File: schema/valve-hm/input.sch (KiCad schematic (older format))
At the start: 5 parts, among them Q1 bc847

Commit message: Разводка платы.
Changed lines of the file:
@@
-EESchema Schematic File Version 2  date 15/06/2012 18:13:53
+EESchema Schematic File Version 2  date Sat 16 Jun 2012 11:54:35 AM MSK
 LIBS:power
 LIBS:device
@@
 Sheet 7 7
 Title ""
-Date "15 jun 2012"
+Date "16 jun 2012"
 Rev ""
 Comp ""
@@
 AR Path="/4FDB3921/4FDB399C" Ref="#PWR056"  Part="1"
 AR Path="/4FDB299D/4FDB399C" Ref="#PWR065"  Part="1"
-F 0 "#PWR065" H 5800 2150 30  0001 C CNN
+F 0 "#PWR050" H 5800 2150 30  0001 C CNN
 F 1 "VDD" H 5800 2160 30  0000 C CNN
 	1    5800 2050
@@
 AR Path="/4FDB3921/4FDB2AE7" Ref="R34"  Part="1"
 AR Path="/4FDB299D/4FDB2AE7" Ref="R42"  Part="1"
-F 0 "R42" V 5880 2550 50  0000 C CNN
+F 0 "R26" V 5880 2550 50  0000 C CNN
 F 1 "33k" V 5800 2550 50  0000 C CNN
 	1    5800 2550
@@
 AR Path="/4FDB3921/4FDB2AA4" Ref="R35"  Part="1"
 AR Path="/4FDB299D/4FDB2AA4" Ref="R43"  Part="1"
-F 0 "R43" V 6580 3250 50  0000 C CNN
+F 0 "R27" V 6580 3250 50  0000 C CNN
 F 1 "2k4" V 6500 3250 50  0000 C CNN
 	1    6500 3250
@@
 AR Path="/4FDB3921/4FDB2A6B" Ref="#PWR057"  Part="1"
 AR Path="/4FDB299D/4FDB2A6B" Ref="#PWR066"  Part="1"
-F 0 "#PWR066" H 4600 4700 30  0001 C CNN
+F 0 "#PWR051" H 4600 4700 30  0001 C CNN
 F 1 "GND" H 4600 4630 30  0001 C CNN
 	1    4600 4700
@@
 AR Path="/4FDB3921/4FDB2A62" Ref="#PWR058"  Part="1"
 AR Path="/4FDB299D/4FDB2A62" Ref="#PWR067"  Part="1"
-F 0 "#PWR067" H 5800 4550 30  0001 C CNN
+F 0 "#PWR052" H 5800 4550 30  0001 C CNN
 F 1 "GND" H 5800 4480 30  0001 C CNN
 	1    5800 4550
@@
 AR Path="/4FDB3921/4FDB29FE" Ref="R33"  Part="1"
 AR Path="/4FDB299D/4FDB29FE" Ref="R41"  Part="1"
-F 0 "R41" V 5130 3600 50  0000 C CNN
+F 0 "R25" V 5130 3600 50  0000 C CNN
 F 1 "2k4" V 5050 3600 50  0000 C CNN
 	1    5050 3600
@@
 AR Path="/4FDB3921/4FDB29E5" Ref="R32"  Part="1"
 AR Path="/4FDB299D/4FDB29E5" Ref="R40"  Part="1"
-F 0 "R40" V 4680 4250 50  0000 C CNN
+F 0 "R24" V 4680 4250 50  0000 C CNN
 F 1 "33k" V 4600 4250 50  0000 C CNN
 	1    4600 4250
@@
 AR Path="/4FDB3921/4FDB29D2" Ref="Q3"  Part="1"
 AR Path="/4FDB299D/4FDB29D2" Ref="Q8"  Part="1"
-F 0 "Q8" H 5700 3450 50  0000 R CNN
+F 0 "Q1" H 5700 3450 50  0000 R CNN
 F 1 "bc847" H 5700 3750 50  0000 R CNN
 	1    5700 3600

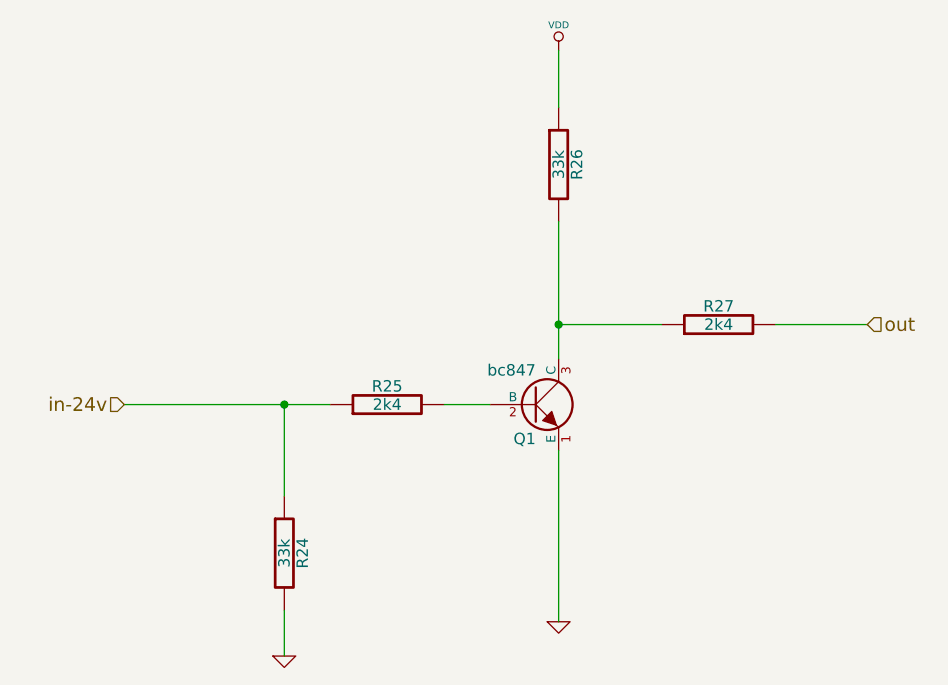
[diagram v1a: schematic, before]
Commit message: Valve-hm is ready. It's digital IO board which can control up to 20 io pins. It is rquipt with 3 LEDs, 2 operating mode switches, USB port and TWI interface.
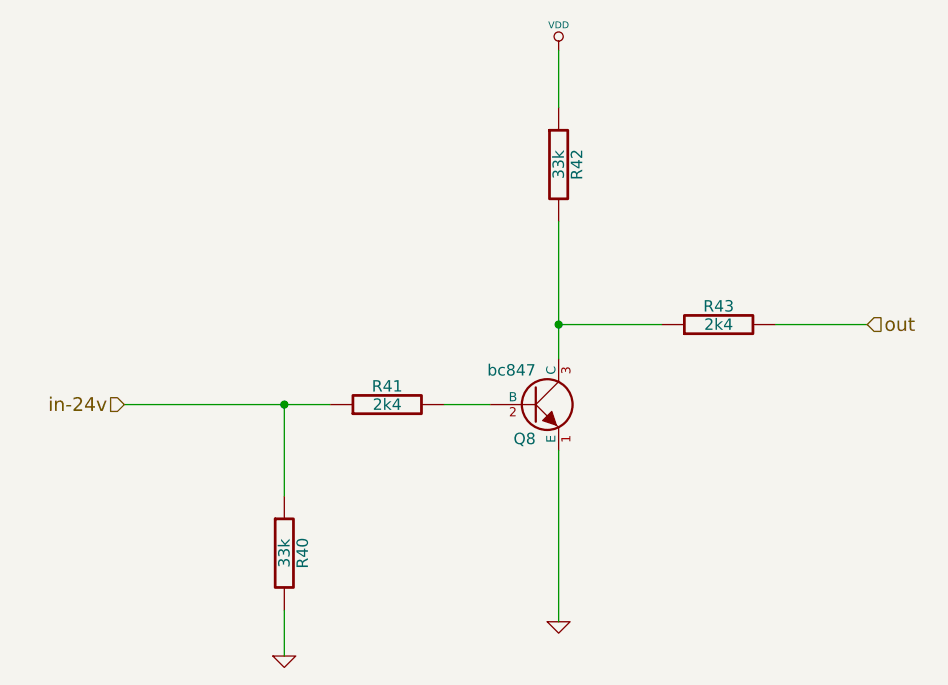
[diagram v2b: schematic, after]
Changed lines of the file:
@@
-EESchema Schematic File Version 2  date Sat 16 Jun 2012 11:54:35 AM MSK
+EESchema Schematic File Version 2  date Sat 16 Jun 2012 01:43:09 PM MSK
 LIBS:power
 LIBS:device
@@
 $EndDescr
 $Comp
-L VDD #PWR050
+L VDD #PWR049
 U 1 1 4FDB399C
 P 5800 2050
-AR Path="/4FDB3936/4FDB399C" Ref="#PWR050"  Part="1"
-AR Path="/4FDB3935/4FDB399C" Ref="#PWR053"  Part="1"
-AR Path="/4FDB3921/4FDB399C" Ref="#PWR056"  Part="1"
-AR Path="/4FDB299D/4FDB399C" Ref="#PWR065"  Part="1"
-F 0 "#PWR050" H 5800 2150 30  0001 C CNN
+AR Path="/4FDB3936/4FDB399C" Ref="#PWR049"  Part="1"
+AR Path="/4FDB3935/4FDB399C" Ref="#PWR052"  Part="1"
+AR Path="/4FDB3921/4FDB399C" Ref="#PWR055"  Part="1"
+AR Path="/4FDB299D/4FDB399C" Ref="#PWR068"  Part="1"
+F 0 "#PWR068" H 5800 2150 30  0001 C CNN
 F 1 "VDD" H 5800 2160 30  0000 C CNN
 	1    5800 2050
@@
 AR Path="/4FDB3921/4FDB2AE7" Ref="R34"  Part="1"
 AR Path="/4FDB299D/4FDB2AE7" Ref="R42"  Part="1"
-F 0 "R26" V 5880 2550 50  0000 C CNN
+F 0 "R42" V 5880 2550 50  0000 C CNN
 F 1 "33k" V 5800 2550 50  0000 C CNN
 	1    5800 2550
@@
 AR Path="/4FDB3921/4FDB2AA4" Ref="R35"  Part="1"
 AR Path="/4FDB299D/4FDB2AA4" Ref="R43"  Part="1"
-F 0 "R27" V 6580 3250 50  0000 C CNN
+F 0 "R43" V 6580 3250 50  0000 C CNN
 F 1 "2k4" V 6500 3250 50  0000 C CNN
 	1    6500 3250
@@
 $EndComp
 $Comp
-L GND #PWR051
+L GND #PWR050
 U 1 1 4FDB2A6B
 P 4600 4700
-AR Path="/4FDB3936/4FDB2A6B" Ref="#PWR051"  Part="1"
-AR Path="/4FDB3935/4FDB2A6B" Ref="#PWR054"  Part="1"
-AR Path="/4FDB3921/4FDB2A6B" Ref="#PWR057"  Part="1"
-AR Path="/4FDB299D/4FDB2A6B" Ref="#PWR066"  Part="1"
-F 0 "#PWR051" H 4600 4700 30  0001 C CNN
+AR Path="/4FDB3936/4FDB2A6B" Ref="#PWR050"  Part="1"
+AR Path="/4FDB3935/4FDB2A6B" Ref="#PWR053"  Part="1"
+AR Path="/4FDB3921/4FDB2A6B" Ref="#PWR056"  Part="1"
+AR Path="/4FDB299D/4FDB2A6B" Ref="#PWR069"  Part="1"
+F 0 "#PWR069" H 4600 4700 30  0001 C CNN
 F 1 "GND" H 4600 4630 30  0001 C CNN
 	1    4600 4700
@@
 $EndComp
 $Comp
-L GND #PWR052
+L GND #PWR051
 U 1 1 4FDB2A62
 P 5800 4550
-AR Path="/4FDB3936/4FDB2A62" Ref="#PWR052"  Part="1"
-AR Path="/4FDB3935/4FDB2A62" Ref="#PWR055"  Part="1"
-AR Path="/4FDB3921/4FDB2A62" Ref="#PWR058"  Part="1"
-AR Path="/4FDB299D/4FDB2A62" Ref="#PWR067"  Part="1"
-F 0 "#PWR052" H 5800 4550 30  0001 C CNN
+AR Path="/4FDB3936/4FDB2A62" Ref="#PWR051"  Part="1"
+AR Path="/4FDB3935/4FDB2A62" Ref="#PWR054"  Part="1"
+AR Path="/4FDB3921/4FDB2A62" Ref="#PWR057"  Part="1"
+AR Path="/4FDB299D/4FDB2A62" Ref="#PWR070"  Part="1"
+F 0 "#PWR070" H 5800 4550 30  0001 C CNN
 F 1 "GND" H 5800 4480 30  0001 C CNN
 	1    5800 4550
@@
 AR Path="/4FDB3921/4FDB29FE" Ref="R33"  Part="1"
 AR Path="/4FDB299D/4FDB29FE" Ref="R41"  Part="1"
-F 0 "R25" V 5130 3600 50  0000 C CNN
+F 0 "R41" V 5130 3600 50  0000 C CNN
 F 1 "2k4" V 5050 3600 50  0000 C CNN
 	1    5050 3600
@@
 AR Path="/4FDB3921/4FDB29E5" Ref="R32"  Part="1"
 AR Path="/4FDB299D/4FDB29E5" Ref="R40"  Part="1"
-F 0 "R24" V 4680 4250 50  0000 C CNN
+F 0 "R40" V 4680 4250 50  0000 C CNN
 F 1 "33k" V 4600 4250 50  0000 C CNN
 	1    4600 4250
@@
 AR Path="/4FDB3921/4FDB29D2" Ref="Q3"  Part="1"
 AR Path="/4FDB299D/4FDB29D2" Ref="Q8"  Part="1"
-F 0 "Q1" H 5700 3450 50  0000 R CNN
+F 0 "Q8" H 5700 3450 50  0000 R CNN
 F 1 "bc847" H 5700 3750 50  0000 R CNN
 	1    5700 3600
